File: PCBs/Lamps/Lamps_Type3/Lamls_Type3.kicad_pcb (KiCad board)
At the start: 2 copper layers, 40.6 x 69.8 mm, 35 parts, among them J1 IN, J2 POWER, J3 LAMP2, J4 LAMP3, J5 LAMP4, J6 LAMP1, J7 LAMP5, J8 LAMP6, Q1 2N2222, Q2 2N2222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

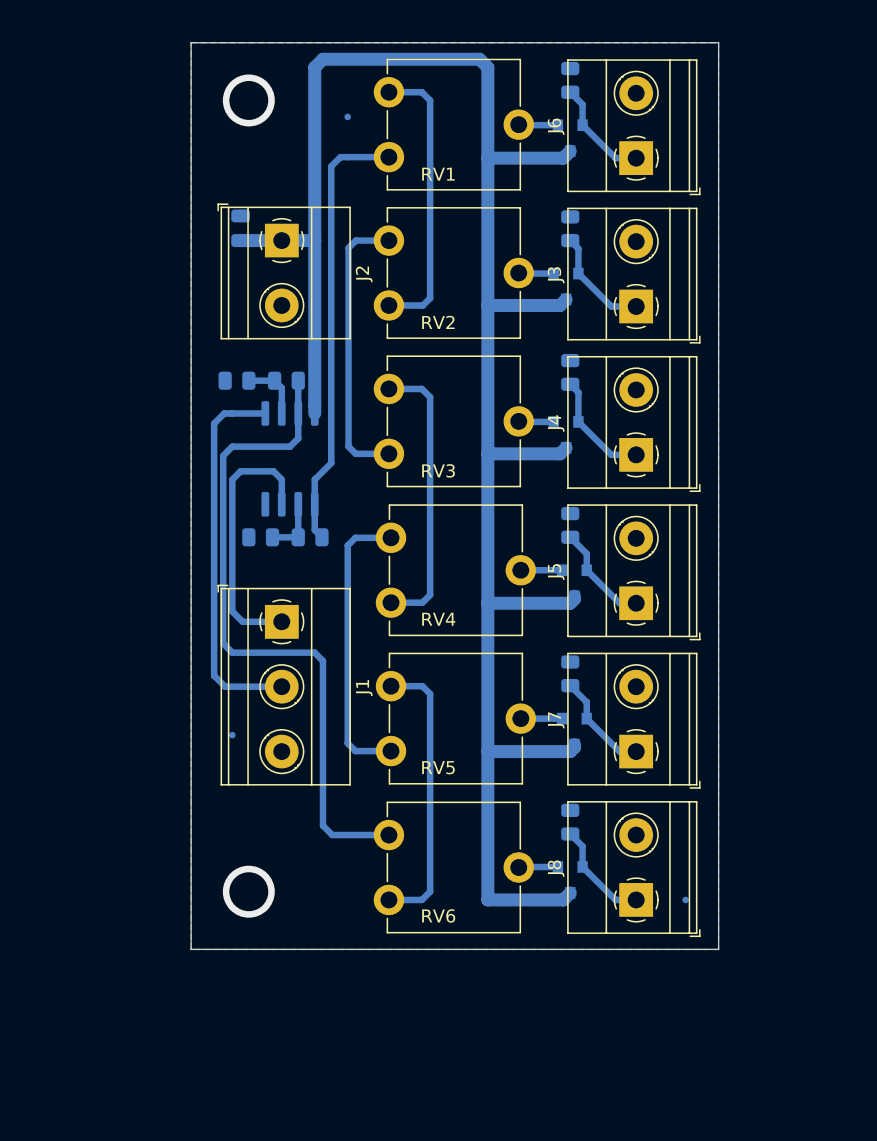
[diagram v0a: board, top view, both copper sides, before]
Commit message: Add LAMPS data
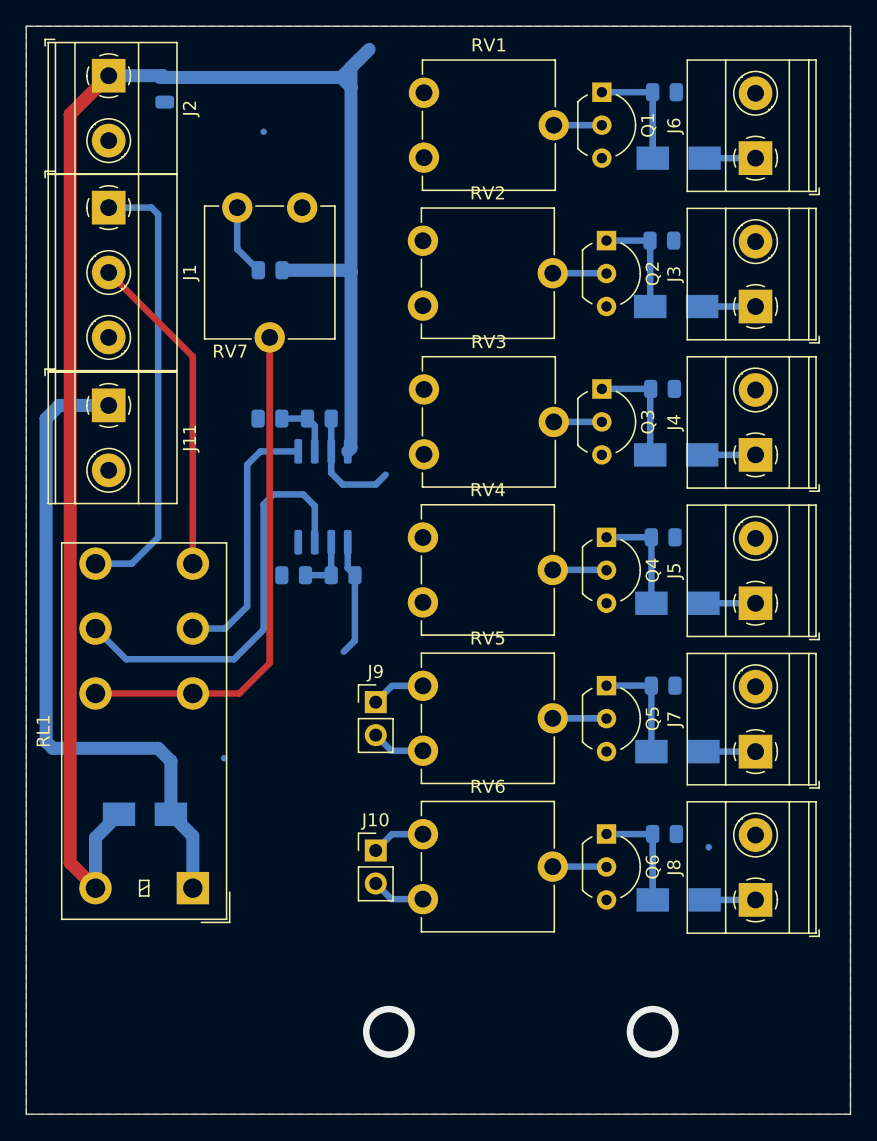
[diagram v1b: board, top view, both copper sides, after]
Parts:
- added D1: 1N4007, Diode_SMD:D_SMA, B.Cu at (182.3, 69.8)
- added D2: 1N4007, Diode_SMD:D_SMA, B.Cu at (182.2, 81.3)
- added D3: 1N4007, Diode_SMD:D_SMA, B.Cu at (182.2, 92.7)
- added D4: 1N4007, Diode_SMD:D_SMA, B.Cu at (182.2, 104.1)
- added D5: 1N4007, Diode_SMD:D_SMA, B.Cu at (182.2, 115.6)
- added D6: 1N4007, Diode_SMD:D_SMA, B.Cu at (182.3, 127.0)
- added D7: 1N4007, Diode_SMD:D_SMA, B.Cu at (141.2, 120.4)
- added J10: 5 CH, Connector_PinHeader_2.54mm:PinHeader_1x02_P2.54mm_Vertical, F.Cu at (159.0, 123.2)
- added J11: ENABLE, TerminalBlock_Phoenix:TerminalBlock_Phoenix_MKDS-1,5-2_1x02_P5.00mm_Horizontal, F.Cu at (138.4, 88.9)
- added J9: 4 CH, Connector_PinHeader_2.54mm:PinHeader_1x02_P2.54mm_Vertical, F.Cu at (159.0, 111.8)
- added R11: 1k, Resistor_SMD:R_0805_2012Metric, B.Cu at (150.9, 78.5)
- added RL1: G2RL-2-ASI-DC12, Relay_THT:Relay_DPDT_Omron_G2RL, F.Cu at (144.9, 126.1)
- added RV7: 20k, Potentiometer_THT:Potentiometer_ACP_CA9-V10_Vertical, F.Cu at (148.3, 73.7)
- Q1, Q2, Q3, Q4, Q5, Q6: footprint Package_TO_SOT_SMD:SOT-23 -> Package_TO_SOT_THT:TO-92_Inline_Wide; moved to F.Cu
- moved J1 34.6 mm to (138.4, 73.7)
- moved J2 18.4 mm to (138.4, 63.5)
- moved C1 12.2 mm to (142.7, 64.6), turned to -90 degrees
- moved J3 9.19 mm to (188.3, 81.3)
- moved J4 9.19 mm to (188.3, 92.7)
- moved J5 9.19 mm to (188.3, 104.1)
- moved J6 9.19 mm to (188.3, 69.8)
- moved J7 9.19 mm to (188.3, 115.6)
- moved J8 9.19 mm to (188.3, 127.0)
- moved R10 7.32 mm to (181.3, 121.9), turned to 0 degrees
- moved R5 7.32 mm to (181.3, 64.8), turned to 0 degrees
- moved R7 7.22 mm to (181.1, 87.6), turned to 0 degrees
- moved R8 7.22 mm to (181.2, 99.1), turned to 0 degrees
- moved R9 7.22 mm to (181.2, 110.5), turned to 0 degrees
- moved R6 7.12 mm to (181.0, 76.2), turned to 0 degrees
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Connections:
- J1 pad 1: Net-(J1-Pad1) -> Net-(RL1-Pad5)
- J1 pad 2: Net-(J1-Pad2) -> Net-(RL1-Pad4)
- Q1 pad 1: Net-(Q1-Pad1) -> Net-(D1-Pad2)
- Q1 pad 2: Net-(J6-Pad1) -> Net-(Q1-Pad2)
- Q2 pad 1: Net-(Q2-Pad1) -> Net-(D2-Pad2)
- Q2 pad 2: Net-(J3-Pad1) -> Net-(Q2-Pad2)
- Q3 pad 1: Net-(Q3-Pad1) -> Net-(D3-Pad2)
- Q3 pad 2: Net-(J4-Pad1) -> Net-(Q3-Pad2)
- Q4 pad 1: Net-(Q4-Pad1) -> Net-(D4-Pad2)
- Q4 pad 2: Net-(J5-Pad1) -> Net-(Q4-Pad2)
- Q5 pad 1: Net-(Q5-Pad1) -> Net-(D5-Pad2)
- Q5 pad 2: Net-(J7-Pad1) -> Net-(Q5-Pad2)
- Q6 pad 1: Net-(Q6-Pad1) -> Net-(D6-Pad2)
- Q6 pad 2: Net-(J8-Pad1) -> Net-(Q6-Pad2)
- R10 pad 1: Net-(J8-Pad1) -> Net-(D6-Pad2)
- R3 pad 2: Net-(R3-Pad2) -> Net-(J10-Pad2)
- R4 pad 2: Net-(R4-Pad2) -> Net-(RV1-Pad3)
- R5 pad 1: Net-(J6-Pad1) -> Net-(D1-Pad2)
- R6 pad 1: Net-(J3-Pad1) -> Net-(D2-Pad2)
- R7 pad 1: Net-(J4-Pad1) -> Net-(D3-Pad2)
- R8 pad 1: Net-(J5-Pad1) -> Net-(D4-Pad2)
- R9 pad 1: Net-(J7-Pad1) -> Net-(D5-Pad2)
- RV1 pad 1: Net-(R3-Pad2) -> Net-(RV1-Pad1)
- RV1 pad 2: Net-(Q1-Pad1) -> Net-(Q1-Pad2)
- RV2 pad 1: Net-(RV1-Pad3) -> Net-(RV2-Pad1)
- RV2 pad 2: Net-(Q2-Pad1) -> Net-(Q2-Pad2)
- RV2 pad 3: Net-(RV2-Pad3) -> Net-(RV1-Pad1)
- RV3 pad 1: Net-(RV2-Pad3) -> Net-(RV3-Pad1)
- RV3 pad 2: Net-(Q3-Pad1) -> Net-(Q3-Pad2)
- RV3 pad 3: Net-(RV3-Pad3) -> Net-(RV2-Pad1)
- RV4 pad 1: Net-(RV3-Pad3) -> Net-(J9-Pad1)
- RV4 pad 2: Net-(Q4-Pad1) -> Net-(Q4-Pad2)
- RV4 pad 3: Net-(RV4-Pad3) -> Net-(RV3-Pad1)
- RV5 pad 1: Net-(RV4-Pad3) -> Net-(J10-Pad1)
- RV5 pad 2: Net-(Q5-Pad1) -> Net-(Q5-Pad2)
- RV5 pad 3: Net-(RV5-Pad3) -> Net-(J9-Pad1)
- RV6 pad 1: Net-(RV5-Pad3) -> Net-(J10-Pad2)
- RV6 pad 2: Net-(Q6-Pad1) -> Net-(Q6-Pad2)
- RV6 pad 3: Net-(R4-Pad2) -> Net-(J10-Pad1)
- U1 pad 1: Net-(R3-Pad2) -> Net-(J10-Pad2)
- U1 pad 3: Net-(J1-Pad1) -> Net-(RL1-Pad6)
- U1 pad 5: Net-(J1-Pad2) -> Net-(RL1-Pad3)
- U1 pad 7: Net-(R4-Pad2) -> Net-(RV1-Pad3)
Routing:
- net Net-(R4-Pad2): track 51.6 -> 0.00 mm
- net Net-(RL1-Pad1): track 0.00 -> 50.9 mm
- net Net-(RL1-Pad2): track 0.00 -> 39.5 mm
- net Net-(RL1-Pad5): track 0.00 -> 34.6 mm
- net Net-(R3-Pad2): track 34.1 -> 0.00 mm
- net Net-(RL1-Pad6): track 0.00 -> 32.0 mm
- net Net-(J1-Pad2): track 29.2 -> 0.00 mm
- net Net-(RL1-Pad4): track 0.00 -> 25.1 mm
- net Net-(RV4-Pad3): track 22.4 -> 0.00 mm
- net Net-(RV2-Pad3): track 22.0 -> 0.00 mm
- net Net-(RV5-Pad3): track 21.9 -> 0.00 mm
- net Net-(RV3-Pad3): track 21.9 -> 0.00 mm
- net +12V: track 150.0 -> 129.1 mm
- net Net-(J1-Pad1): track 20.5 -> 0.00 mm
- net Net-(RL1-Pad3): track 0.00 -> 20.2 mm
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- added copper zone on F.Cu, net GND
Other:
- board size 40.6 x 69.8 mm -> 63.5 x 83.8 mm
- net class Default removed
- net class Power removed
- net class Signals removed
